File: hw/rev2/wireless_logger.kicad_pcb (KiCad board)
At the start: 4 copper layers, 30 x 50 mm, 156 parts, among them J1 FCI 10118194, J2 CONN_2, J3 SSD1306_SER, J4 SWD_10PIN, J5 CONN_5, J6 CONN_6X2, Q1 2N7002P, Q2 2N7002P, U1 MT29FXX01A, U10 CC2541, U11 STM32F40X_BGA176, U2 MAG3110, U3 MMA8452Q, U4 LPS331AP, U5 L3GD20, U6 MCP111T-315, U7 BQ24095, U8 TPS62698, U9 CC1101, X1 FA-128 26.0000MF10Z-W3, X2 9HT10-32.768KBZF-T, X3 FA-128 32.0000MF20X-K3, X4 XRCGB25M000F0L00R0, X5 9HT10-32.768KBZF-T

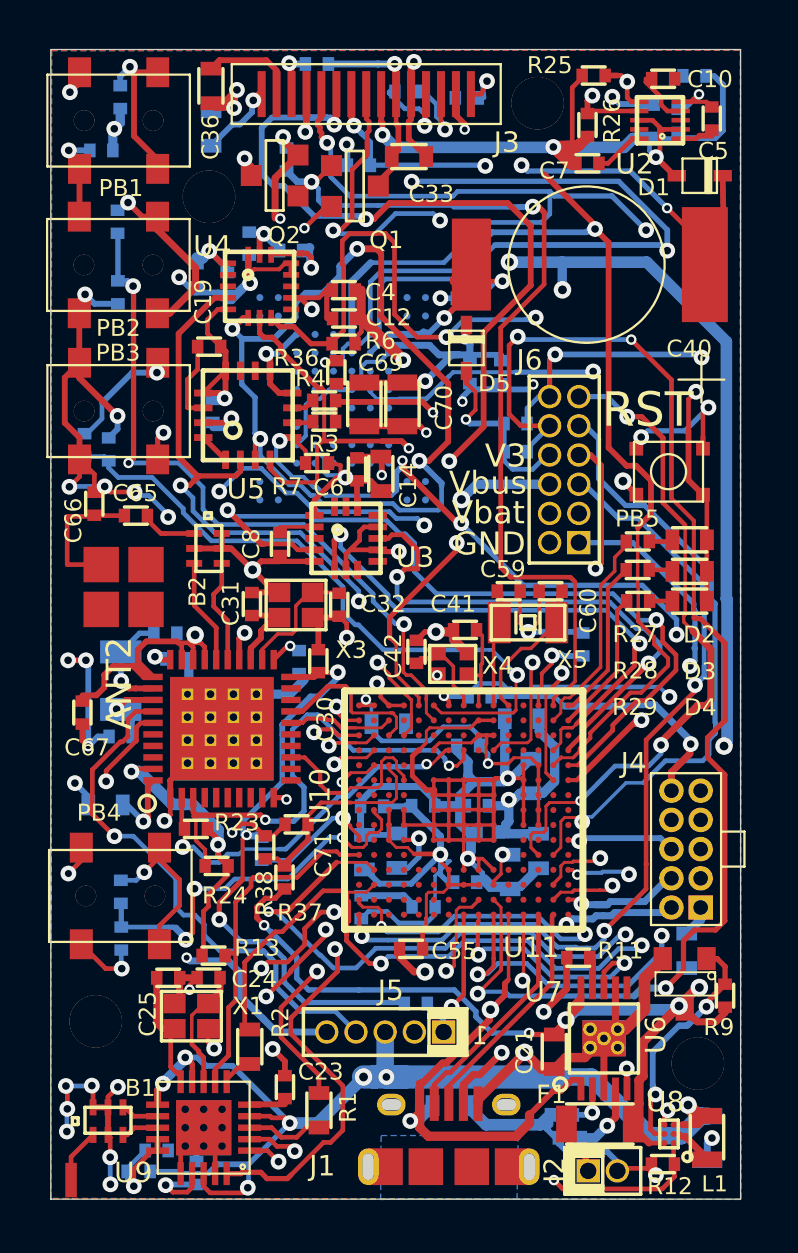
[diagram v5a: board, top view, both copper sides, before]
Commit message: Prepared upgrade to hw rev2c: Changes: 	Larger pads on flash BGA for easier mounting 	Move a few signals that were close to sensitive clock connections 	Remap more things to SPI1, USART1, and USART6 to avoid DMA 		conflicts 	Moved USB connection, fixed milling instructions for mount 	Removed gating of OLED -- not worth it 	Removed supply isolation on flash -- not worth it Additions: 	ADMP521 digital MEMS microphone optionally on SPI2
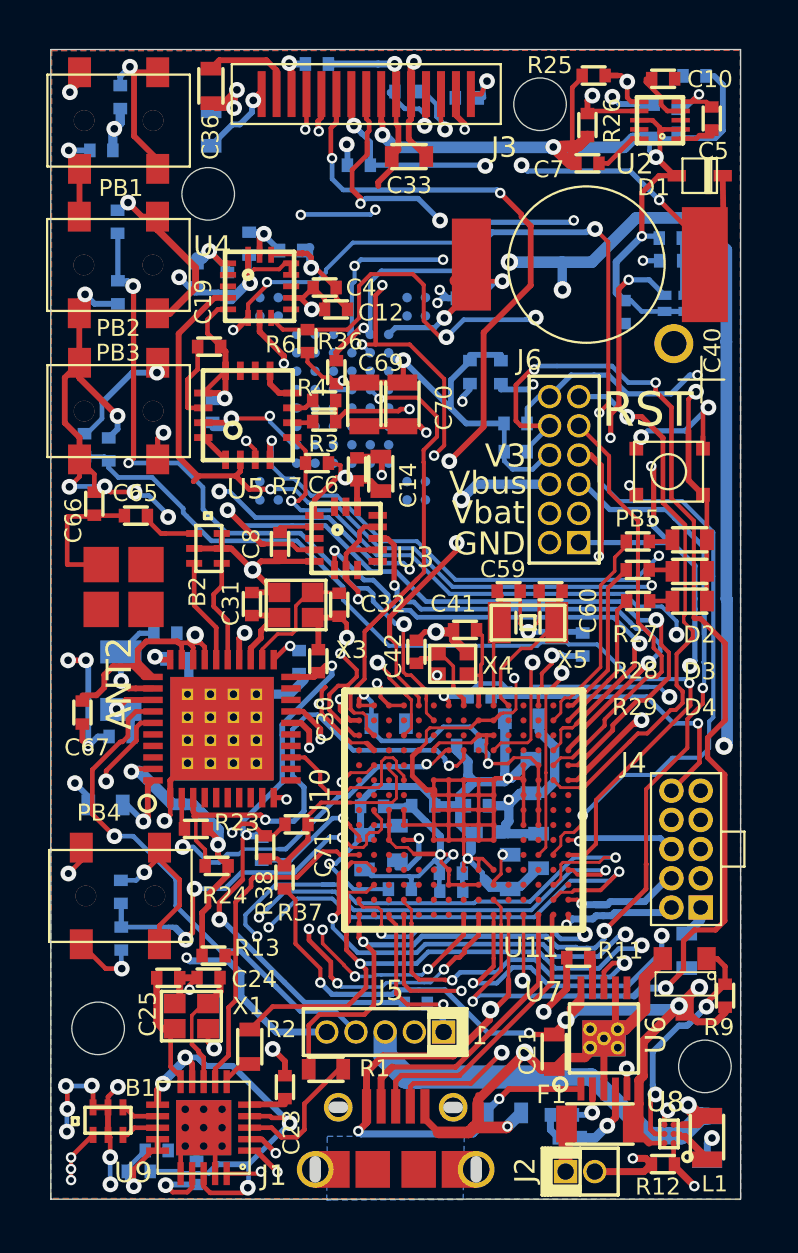
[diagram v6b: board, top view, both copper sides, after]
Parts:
- removed D5: BAT43XV2, SOD-523F
- removed PAD_0_5x1_5: VAL**, PAD_0_5x1_5
- removed Q1, Q2: 2N7002P, SOT23GDS
- removed the SCREW_HOLE_2-56 at (172.0, 152.3)
- removed the SCREW_HOLE_2-56 at (191.2, 112.3)
- removed the SCREW_HOLE_2-56 at (198.1, 154.1)
- removed the SCREW_HOLE_2-56 at (176.9, 116.4)
- removed VAL: MCGILL, MCGILL
- removed VAL: EAGLE, EAGLE
- removed VAL: OSHW, OSHW
- added R39: 1M, SMD0402, B.Cu at (197.0, 118.2)
- added SCREW_HOLE_2-56: VAL**, SCREW_HOLE_2-56, F.Cu at (191.3, 112.4)
- added SCREW_HOLE_2-56: VAL**, SCREW_HOLE_2-56, F.Cu at (198.4, 154.2)
- added SCREW_HOLE_2-56: VAL**, SCREW_HOLE_2-56, F.Cu at (176.8, 116.3)
- added SCREW_HOLE_2-56: VAL**, SCREW_HOLE_2-56, F.Cu at (172.1, 152.6)
- added U12: MEMS_DGTL_MIC, ADMP521, B.Cu at (197.1, 121.8)
- C55: value 10n -> 0.1u; moved to B.Cu
- R19: value 100k -> 0R
- moved C55 29.2 mm to (194.9, 121.4), turned to 90 degrees
- moved R19 17.3 mm to (197.0, 119.2), turned to 0 degrees
- moved C58 3.98 mm to (187.4, 146.6), turned to 180 degrees
- moved C20 2.38 mm to (189.7, 156.2)
- moved J1 2.31 mm to (185.0, 158.7)
- moved R1 1.81 mm to (182.0, 154.4), turned to 180 degrees
- moved R6 1.57 mm to (181.2, 122.7), turned to 270 degrees
- moved C57 1.29 mm to (185.2, 146.5)
- moved J2 0.98 mm to (193.0, 158.8)
- moved C4 0.84 mm to (181.9, 120.4)
- moved C50 0.73 mm to (187.4, 145.8)
- moved C12 0.52 mm to (182.4, 121.3)
- moved C44 0.33 mm to (185.1, 144.5)
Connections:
- net /Sensors/GYR_DRDY/INT2 renamed /Sensors/GYR_DRDY_INT2
- C1 pad 2: /V3_FLASH -> V3
- C2 pad 2: /V3_FLASH -> V3
- C33 pad 1: /OLED/OLED_GND -> GND
- C36 pad 1: /OLED/OLED_GND -> GND
- C37 pad 1: /OLED/OLED_GND -> GND
- C69 pad 2: /V3_FLASH -> V3
- C70 pad 2: /V3_FLASH -> V3
- J3 pad 6: /OLED/OLED_GND -> GND
- J6 pad 11: /STM32F4/UART2_TX -> /STM32F4/USART1_TX
- J6 pad 9: /STM32F4/UART2_RX -> /STM32F4/USART1_RX
- R19 pad 1: GND -> /STM32F4/SPI2_CLK
- R19 pad 2: /OLED/EN -> N-0000036
- R20 pad 1: /OLED/OLED_GND -> GND
- R21 pad 1: /OLED/OLED_GND -> GND
- R36 pad 2: /V3_FLASH -> V3
- U1 pad D3: /V3_FLASH -> V3
- U1 pad G5: /V3_FLASH -> V3
- U1 pad G6: /V3_FLASH -> V3
- U1 pad G7: /STM32F4/SPI3_MISO -> /STM32F4/SPI1_MISO
- U1 pad J8: /V3_FLASH -> V3
- U10 pad 16: /Bluetooth/TX/MOSI -> /Bluetooth/TX_MOSI
- U10 pad 17: /Bluetooth/RX/MISO -> /Bluetooth/RX_MISO
- U11 pad A11: (no net) -> /STM32F4/EXTI7
- U11 pad A12: /OLED/SDIN -> /Sensors/GYR_SPI_MOSI
- U11 pad B1: /OLED/EN -> (no net)
- U11 pad B11: /STM32F4/UART2_RX -> /STM32F4/FLASH_nCS
- U11 pad B13: /STM32F4/SPI3_MISO -> /Sensors/GYR_SPI_MISO
- U11 pad B14: /OLED/SCLK -> /Sensors/GYR_SPI_CLK
- U11 pad B5: /STM32F4/FLASH_nCS -> /STM32F4/USART1_RX
- U11 pad B6: /Sensors/PRS_SPI_nCS -> /STM32F4/USART1_TX
- U11 pad C11: /STM32F4/UART2_TX -> /Sensors/PRS_SPI_nCS
- U11 pad G14: /STM32F4/REG_nUSB_CONN -> (no net)
- U11 pad G15: /STM32F4/REG_nCHG -> /Bluetooth/TX_MOSI
- U11 pad H15: /Power/MODE -> /Bluetooth/RX_MISO
- U11 pad K1: /STM32F4/EXTI7 -> (no net)
- U11 pad M14: (no net) -> /STM32F4/REG_nCHG
- U11 pad M15: (no net) -> /STM32F4/REG_nUSB_CONN
- U11 pad N15: (no net) -> /Power/MODE
- U11 pad N2: /Bluetooth/TX/MOSI -> (no net)
- U11 pad N3: /Bluetooth/RX/MISO -> (no net)
- U11 pad P3: /Sensors/GYR_SPI_MISO -> /STM32F4/SPI1_MISO
- U11 pad P4: /Sensors/GYR_SPI_CLK -> /OLED/SCLK
- U11 pad R3: /Sensors/GYR_SPI_MOSI -> /OLED/SDIN
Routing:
- net /OLED/EN: track 40.8 -> 0.00 mm, vias 2 -> 0
- net /STM32F4/SPI3_MISO: track 36.4 -> 0.00 mm, vias 2 -> 0
- net /OLED/SDIN: track 68.9 -> 39.0 mm, vias 5 -> 7
- net /STM32F4/UART2_TX: track 29.4 -> 0.00 mm, vias 3 -> 0
- net /STM32F4/UART2_RX: track 27.2 -> 0.00 mm, vias 1 -> 0
- net /STM32F4/USART1_TX: track 0.00 -> 24.2 mm, vias 0 -> 1
- net /STM32F4/SPI1_MISO: track 0.00 -> 22.9 mm, vias 0 -> 1
- net /OLED/SCLK: track 64.6 -> 41.8 mm, vias 3 -> 4
- net /Sensors/GYR_SPI_CLK: track 57.4 -> 79.1 mm, vias 6 -> 5
- net /Bluetooth/TX_MOSI: track 0.00 -> 20.6 mm, vias 0 -> 4
- net /OLED/OLED_GND: track 20.2 -> 0.00 mm, vias 5 -> 0
- net /Bluetooth/RX_MISO: track 0.00 -> 19.5 mm, vias 0 -> 4
- net /V3_FLASH: track 19.2 -> 0.00 mm, vias 2 -> 0
- net /Sensors/GYR_SPI_MISO: track 57.0 -> 75.8 mm, vias 5 -> 6
- net /STM32F4/USART1_RX: track 0.00 -> 18.7 mm
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- removed copper zone on GND_PLANE, net /OLED/OLED_GND
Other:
- outline, holes or cut-outs redrawn
- board text added: "r2c"
- board text removed: "r2b"

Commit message: Submitted rev2c for manufacturing
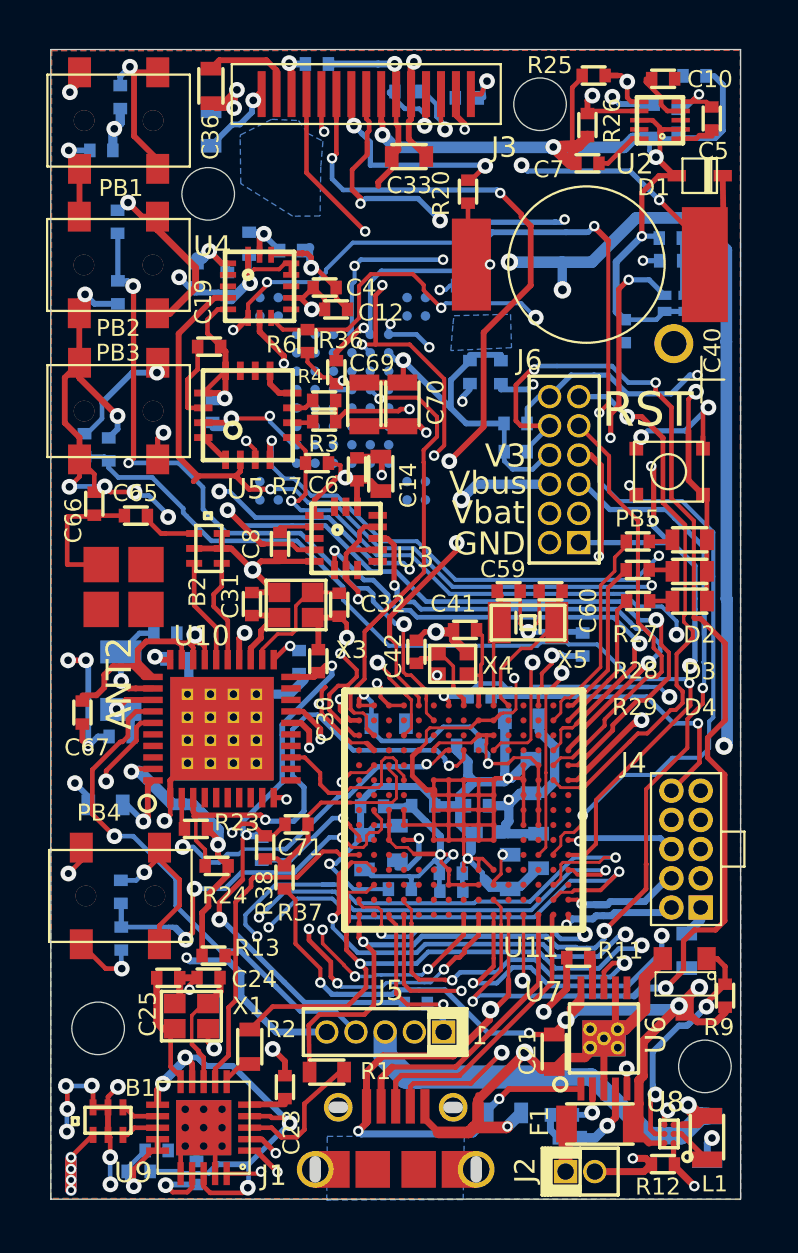
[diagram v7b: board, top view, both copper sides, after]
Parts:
- added PAD_0_5x1_5: VAL**, PAD_0_5x1_5, F.Cu at (170.9, 158.9)
- added VAL: MCGILL, MCGILL, B.Cu at (191.7, 121.7)
- added VAL: EAGLE, EAGLE, B.Cu at (186.1, 115.8)
- R20: moved to F.Cu
- moved R20 4.88 mm to (188.1, 116.2), turned to 90 degrees
- moved C55 0.83 mm to (194.9, 122.3)
- moved C16 0.55 mm to (188.1, 120.3)
- moved R1 0.13 mm to (182.0, 154.5)
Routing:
- net GND: track 298.0 -> 292.5 mm
- net /Guardian Interface/GUARDIAN_ANT_SE: track 2.58 -> 5.36 mm, vias 3 -> 4
- net /OLED/SDIN: track 39.0 -> 36.4 mm, vias 7 -> 5
- net /STM32F4/FLASH_nCS: track 51.4 -> 53.3 mm
- net V3: track 348.1 -> 346.6 mm, vias 29 -> 28
- net /Sensors/PRS_SPI_nCS: track 43.2 -> 41.9 mm
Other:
- board text added: "X"
- board text added: "Y"
- board text added: "Z"

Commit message: Tiny update to bottom silk screen. This acutally made it into the manufacturing of rev2c by email
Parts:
- added VAL: OSHW, OSHW, B.Cu at (176.8, 151.5)
